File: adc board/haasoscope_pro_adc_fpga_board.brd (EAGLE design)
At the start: 224.5 x 160 mm, 580 parts, among them CN2 12Vin, IC1 ADC12DL2500ACF, IC10 TPS72325DBVR, IC13 LMH5401IRMST, IC14 LMH6401IRMZR, IC15 SN74AVC4T774PWR, IC17 DAC8562SDGSR, IC18 TLV9102IPWR, IC2 SN74AVC4T774PWR, IC21 LMH5401IRMST, IC22 TPS7A7200RGTR, IC23 TPS7A7200RGTR, IC24 TPS7A7200RGTR, IC25 TPS72325DBVR, IC26 TPS7A7200RGTR, IC27 TPS7A7200RGTR, IC28 TPS7A7200RGTR, IC29 LMH6401IRMZR, IC3 ADC122S021CIMM_NOPB, IC30 SN74AVC4T774PWR, IC33 TLV9102IPWR, IC4 TLV9102IPWR, IC5 EP4CE30F23C6N, IC6 EPCQ16ASI8N, IC7 TPS7A7200RGTR, IC8 FT232HQ, IC9 93LC56B, J1 2p-2.54, J10 8pin, J11 8pin, J13 8pin, J14 2x5, J15 test1, J2 test1, J3 2p-2.54, J30 2p-2.54, J31 2p-2.54, J32 2p-2.54, J33 2p-2.54, J34 2p-2.54, J35 2p-2.54, J36 2p-2.54, J37 2p-2.54, J39 2p-2.54, J4 2p-2.54, J40 2p-2.54, J41 2p-2.54, J42 2p-2.54, J43 2p-2.54, J44 2p-2.54, J45 2p-2.54, J46 2p-2.54, J8 8pin, K1 G6K-2F-RF-T-TR03_DC5, K2 G6K-2F-RF-T-TR03_DC5, K3 G6K-2F-RF-T-TR03_DC5, K4 G6K-2F-RF-T-TR03_DC5, K5 G6K-2F-RF-T-TR03_DC5, K6 TLP3475R_TP,F, K7 TLP3475R_TP,F, Q1 S8050, Q2 FDN340P, Q4 S8050, Q5 S8050, Q7 S8050, Q8 S8050, Q9 S8050, SW3 SKQGADE010, SW4 SKQGADE010, U2 ADF4350BCPZ, X1 USBC, Y2 OSCILLATORSMD-5X3, Y3 12MHz

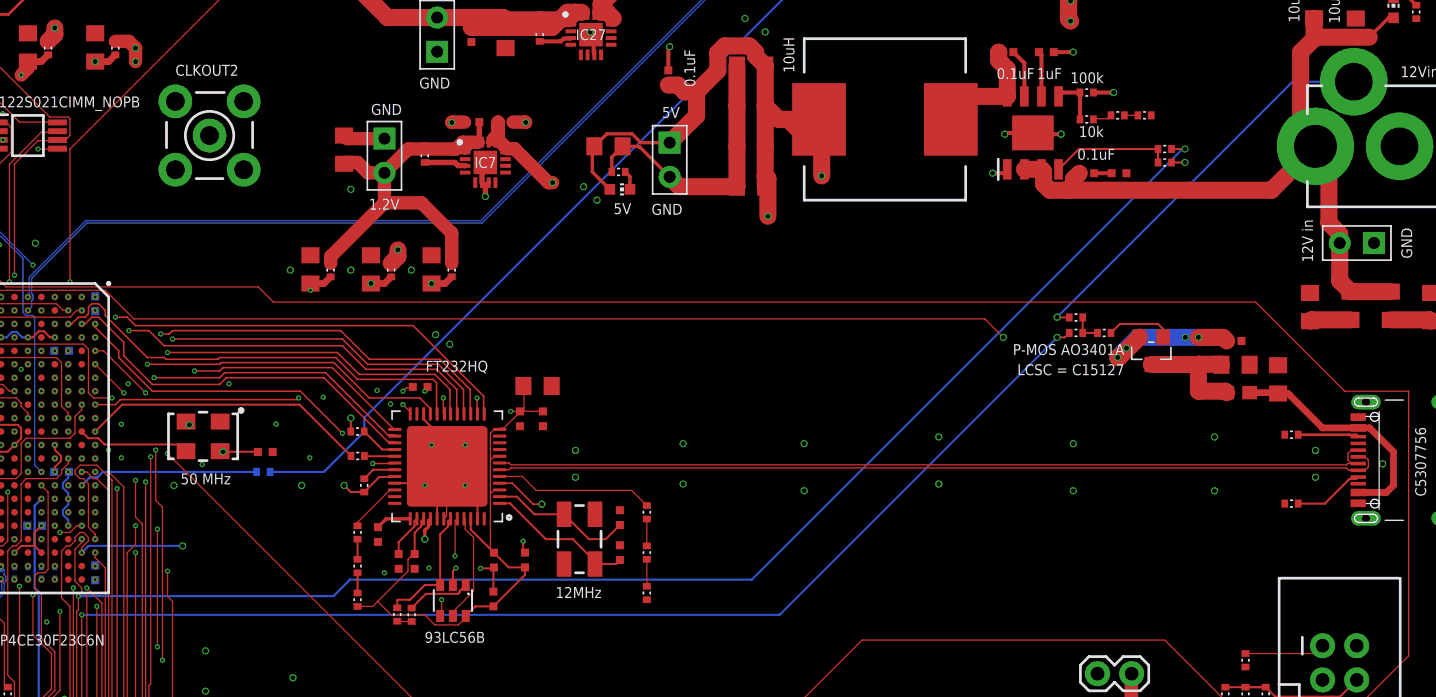
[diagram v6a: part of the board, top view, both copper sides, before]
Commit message: detect 12V and disconnect 5V from USB
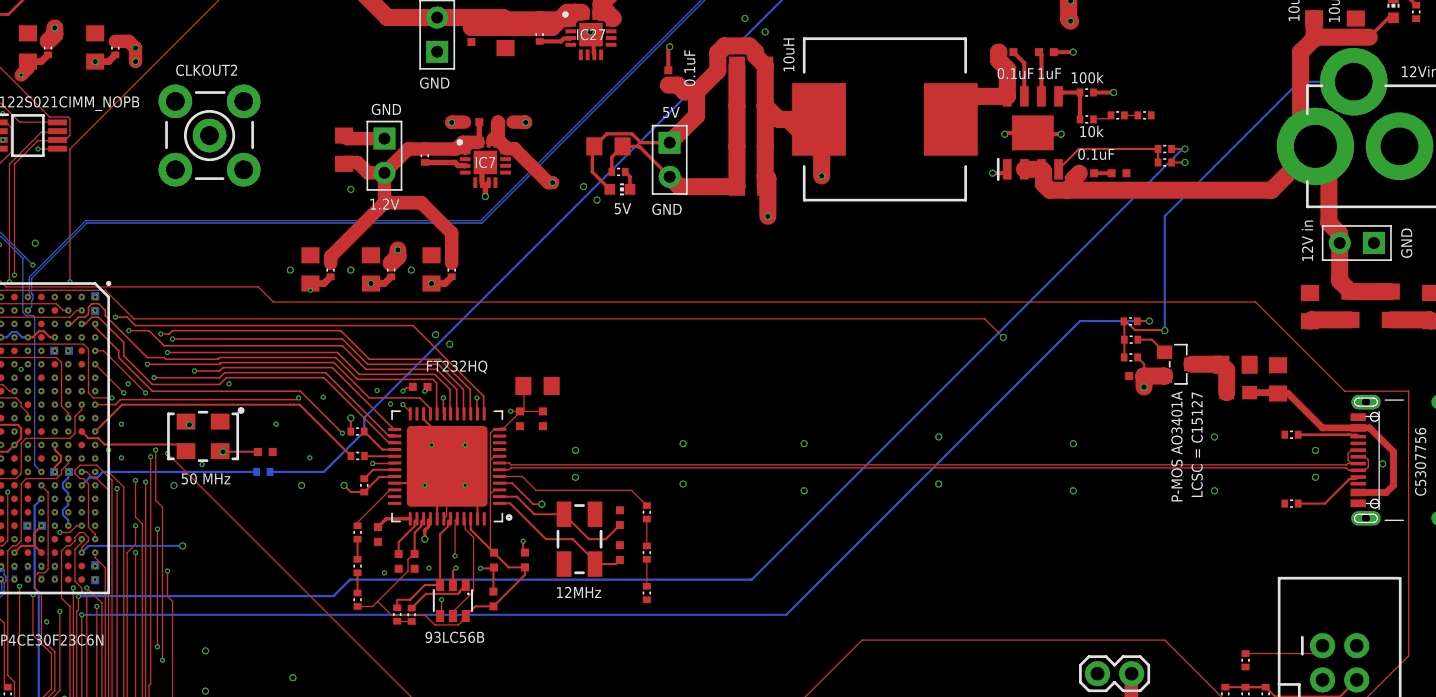
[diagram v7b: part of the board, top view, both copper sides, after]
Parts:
- moved C117 7.71 mm to (199.9, 84.1), turned to 0 degrees
- moved R237 5.05 mm to (199.5, 85.5)
- moved R238 4.15 mm to (199.5, 88.2), turned to 0 degrees
- moved Q2 2.24 mm to (203.0, 85.0), turned to 270 degrees
- moved R239 2.06 mm to (199.5, 86.8)
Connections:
- removed net 12VNOTCONNECTED: R237.P$2, R238.P$1, R239.P$1
- removed net N$64: CN2.GNDBREAK, R237.P$1
- new net 12VCONNECTED: CN2.GNDBREAK, R237.P$1, R238.P$1, R239.P$1
- net 5V: now also R237.P$2
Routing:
- net 12VCONNECTED: track 0.00 -> 32.7 mm, vias 0 -> 1
- net N$64: track 30.2 -> 0.00 mm, vias 1 -> 0
- net BOARDIN2: track 139.9 -> 147.1 mm
- net 5V: track 133.1 -> 126.0 mm, vias 26 -> 23
- net VBUSCLEAN: track 9.38 -> 4.44 mm
- net N$65: track 4.92 -> 2.37 mm
- net 12VNOTCONNECTED: track 2.25 -> 0.00 mm
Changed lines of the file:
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@@
 <element name="C115" library="Nordic_nRF" library_urn="urn:adsk.eagle:library:169009" package="RESC0402_N" package3d_urn="urn:adsk.eagle:package:2593732/1" value="0.1uF" x="143.517" y="72.347" smashed="yes" rot="R90"/>
 <element name="C116" library="Nordic_nRF" library_urn="urn:adsk.eagle:library:169009" package="RESC0402_N" package3d_urn="urn:adsk.eagle:package:2593732/1" value="0.1uF" x="154.0735" y="80.947" smashed="yes" rot="R90"/>
-<element name="C117" library="Nordic_nRF" library_urn="urn:adsk.eagle:library:169009" package="RESC0402_N" package3d_urn="urn:adsk.eagle:package:2593732/1" value="0.1uF" x="207.153" y="86.7345" smashed="yes" rot="R180"/>
+<element name="C117" library="Nordic_nRF" library_urn="urn:adsk.eagle:library:169009" package="RESC0402_N" package3d_urn="urn:adsk.eagle:package:2593732/1" value="0.1uF" x="199.897" y="84.1255" smashed="yes"/>
 <element name="C118" library="Nordic_nRF" library_urn="urn:adsk.eagle:library:169009" package="RESC0805_N" package3d_urn="urn:adsk.eagle:package:2593736/1" value="10uF" x="210.4235" y="83.8275" smashed="yes" rot="R270"/>
 <element name="C119" library="Nordic_nRF" library_urn="urn:adsk.eagle:library:169009" package="RESC0402_N" package3d_urn="urn:adsk.eagle:package:2593732/1" value="0.1uF" x="146.2455" y="70.347" smashed="yes" rot="R90"/>
@@
 <element name="R212" library="FlashPCB_Resistors" package="RES-0402" value="10k" x="202" y="100" smashed="yes" rot="R180"/>
 <element name="R236" library="FlashPCB_Resistors" package="RES-0402" value="1k" x="202" y="101" smashed="yes"/>
-<element name="Q2" library="Seeed-Transistor" library_urn="urn:adsk.eagle:library:477" package="SOT-23" package3d_urn="urn:adsk.eagle:package:33015/1" value="FDN340P" x="201" y="86" smashed="yes" rot="R180">
-<attribute name="LCSC" value="C15127" x="199" y="85" size="0.8128" layer="21" rot="R180" display="both"/>
-<attribute name="MPN" value="P-MOS AO3401A" x="199" y="86.5" size="0.8128" layer="21" rot="R180"/>
-</element>
-<element name="R237" library="FlashPCB_Resistors" package="RES-0402" value="10k" x="195.4" y="88.48" smashed="yes"/>
-<element name="R238" library="FlashPCB_Resistors" package="RES-0402" value="1k" x="195.4" y="87.33" smashed="yes" rot="R180"/>
-<element name="R239" library="FlashPCB_Resistors" package="RES-0402" value="10k" x="197.5" y="87.33" smashed="yes"/>
+<element name="Q2" library="Seeed-Transistor" library_urn="urn:adsk.eagle:library:477" package="SOT-23" package3d_urn="urn:adsk.eagle:package:33015/1" value="FDN340P" x="203" y="85" smashed="yes" rot="R270">
+<attribute name="LCSC" value="C15127" x="204" y="83" size="0.8128" layer="21" rot="R270" display="both"/>
+<attribute name="MPN" value="P-MOS AO3401A" x="202.5" y="83" size="0.8128" layer="21" rot="R270"/>
+</element>
+<element name="R237" library="FlashPCB_Resistors" package="RES-0402" value="10k" x="199.48" y="85.51" smashed="yes"/>
+<element name="R238" library="FlashPCB_Resistors" package="RES-0402" value="1k" x="199.46" y="88.19" smashed="yes"/>
+<element name="R239" library="FlashPCB_Resistors" package="RES-0402" value="10k" x="199.5" y="86.83" smashed="yes"/>
 </elements>
 <signals>
@@
 <via x="121.5" y="29.875" extent="1-16" drill="0.2"/>
 <contactref element="R238" pad="P$2"/>
-<wire x1="194.9" y1="87.33" x2="194.57" y2="87" width="0.1524" layer="1"/>
-<wire x1="194.57" y1="87" x2="194" y2="87" width="0.1524" layer="1"/>
-<via x="194" y="87" extent="1-16" drill="0.35"/>
-<wire x1="194" y1="87" x2="173.375" y2="66.375" width="0.1524" layer="16"/>
-<wire x1="173.375" y1="66.375" x2="121.5" y2="66.375" width="0.1524" layer="16"/>
+<via x="200.86" y="88.21" extent="1-16" drill="0.35"/>
+<wire x1="200.86" y1="88.21" x2="195.71" y2="88.21" width="0.1524" layer="16"/>
+<wire x1="195.71" y1="88.21" x2="173.875" y2="66.375" width="0.1524" layer="16"/>
+<wire x1="173.875" y1="66.375" x2="121.5" y2="66.375" width="0.1524" layer="16"/>
+<wire x1="199.96" y1="88.19" x2="199.98" y2="88.21" width="0.1524" layer="1"/>
+<wire x1="200.86" y1="88.21" x2="199.98" y2="88.21" width="0.1524" layer="1"/>
 </signal>
 <signal name="BOARDIN3">
@@
 <vertex x="-9.5" y="-11.5"/>
 </polygon>
-<via x="204.5" y="87" extent="1-16" drill="0.35"/>
+<via x="200.46" y="83.31" extent="1-16" drill="0.35"/>
 <via x="172.5" y="96" extent="1-16" drill="0.35"/>
 <via x="176.5" y="99" extent="1-16" drill="0.35"/>
@@
 <wire x1="194.85615" y1="110.64385" x2="195" y2="110.5" width="1.27" layer="1"/>
 <contactref element="JST_FAN" pad="1"/>
-<wire x1="204.5" y1="87" x2="206.3375" y2="87" width="1.27" layer="1"/>
-<wire x1="206.3375" y1="87" x2="206.603" y2="86.7345" width="1.27" layer="1"/>
+<wire x1="200.447" y1="84.1255" x2="200.46" y2="84.1125" width="1.27" layer="1"/>
+<wire x1="200.46" y1="84.1125" x2="200.46" y2="83.31" width="1.27" layer="1"/>
 <contactref element="K1" pad="1"/>
 <contactref element="K2" pad="1"/>
@@
 <wire x1="200.8" y1="17.7" x2="200.8" y2="13.47" width="1.016" layer="1"/>
 <contactref element="Q2" pad="2"/>
-<wire x1="200.111" y1="87.016" x2="198.595" y2="85.5" width="1.27" layer="1"/>
-<wire x1="198.595" y1="85.5" x2="198.5" y2="85.5" width="1.27" layer="1"/>
-<via x="198.5" y="85.5" extent="1-16" drill="0.35"/>
-<wire x1="198.5" y1="85.5" x2="200" y2="87" width="1.27" layer="16"/>
-<wire x1="200" y1="87" x2="204.5" y2="87" width="1.27" layer="16"/>
-<via x="199.15" y="86.2" extent="1-16" drill="0.35"/>
-<via x="203.53" y="87" extent="1-16" drill="0.35"/>
+<contactref element="R237" pad="P$2"/>
+<wire x1="199.98" y1="85.51" x2="200.46" y2="85.03" width="0.1524" layer="1"/>
+<wire x1="200.46" y1="85.03" x2="200.46" y2="84.1125" width="0.1524" layer="1"/>
+<wire x1="200.447" y1="84.1255" x2="201.9695" y2="84.1255" width="1.27" layer="1"/>
+<wire x1="201.9695" y1="84.1255" x2="201.984" y2="84.111" width="1.27" layer="1"/>
 </signal>
 <signal name="COIL1-">
@@
 <contactref element="FB2" pad="2"/>
 <contactref element="C126" pad="2"/>
-<wire x1="204.5" y1="85" x2="206.1725" y2="85" width="1.27" layer="1"/>
-<wire x1="206.1725" y1="85" x2="206.2085" y2="84.964" width="1.27" layer="1"/>
-<wire x1="204.5" y1="83" x2="206.496" y2="83" width="1.27" layer="1"/>
-<wire x1="206.496" y1="83" x2="206.6045" y2="82.8915" width="1.27" layer="1"/>
 <contactref element="Q2" pad="3"/>
-<wire x1="204.5" y1="85" x2="204.484" y2="84.984" width="1.27" layer="1"/>
-<wire x1="204.484" y1="84.984" x2="201" y2="84.984" width="1.27" layer="1"/>
-<wire x1="204.5" y1="85" x2="204.5" y2="83" width="1.27" layer="1"/>
+<wire x1="204.016" y1="85" x2="206.1725" y2="85" width="1.27" layer="1"/>
+<wire x1="206.1725" y1="85" x2="206.2085" y2="84.964" width="1.27" layer="1"/>
+<wire x1="206.2085" y1="84.964" x2="206.6045" y2="84.568" width="1.27" layer="1"/>
+<wire x1="206.6045" y1="84.568" x2="206.6045" y2="82.8915" width="1.27" layer="1"/>
 </signal>
-<signal name="12VNOTCONNECTED">
-<contactref element="R237" pad="P$2"/>
+<signal name="12VCONNECTED">
 <contactref element="R238" pad="P$1"/>
 <contactref element="R239" pad="P$1"/>
-<wire x1="195.9" y1="88.48" x2="195.9" y2="87.33" width="0.1524" layer="1"/>
-<wire x1="195.9" y1="87.33" x2="197" y2="87.33" width="0.1524" layer="1"/>
-</signal>
-<signal name="N$64">
 <contactref element="CN2" pad="GNDBREAK"/>
 <contactref element="R237" pad="P$1"/>
-<wire x1="194.9" y1="88.48" x2="194.02" y2="88.48" width="0.1524" layer="1"/>
-<wire x1="194.02" y1="88.48" x2="194" y2="88.5" width="0.1524" layer="1"/>
-<via x="194" y="88.5" extent="1-16" drill="0.35"/>
-<wire x1="194" y1="88.5" x2="211.5" y2="106" width="0.1524" layer="16"/>
-<wire x1="211.5" y1="106" x2="216.05" y2="106" width="0.1524" layer="16"/>
+<via x="202" y="87.5" extent="1-16" drill="0.35"/>
+<wire x1="216.05" y1="106" x2="212" y2="106" width="0.1524" layer="16"/>
+<wire x1="212" y1="106" x2="202" y2="96" width="0.1524" layer="16"/>
+<wire x1="202" y1="96" x2="202" y2="87.5" width="0.1524" layer="16"/>
+<wire x1="198.96" y1="88.19" x2="199" y2="88.15" width="0.1524" layer="1"/>
+<wire x1="199" y1="88.15" x2="199" y2="86.83" width="0.1524" layer="1"/>
+<wire x1="199" y1="86.83" x2="199" y2="85.53" width="0.1524" layer="1"/>
+<wire x1="199" y1="85.53" x2="198.98" y2="85.51" width="0.1524" layer="1"/>
+<wire x1="199.16263125" y1="88.15" x2="199" y2="88.15" width="0.1524" layer="1"/>
+<wire x1="202" y1="87.5" x2="201.9582" y2="87.5418" width="0.1524" layer="1"/>
+<wire x1="201.9582" y1="87.5418" x2="199.77083125" y2="87.5418" width="0.1524" layer="1"/>
+<wire x1="199.77083125" y1="87.5418" x2="199.16263125" y2="88.15" width="0.1524" layer="1"/>
 </signal>
 <signal name="N$65">
 <contactref element="Q2" pad="1"/>
 <contactref element="R239" pad="P$2"/>
-<wire x1="198" y1="87.33" x2="198.67" y2="88" width="0.1524" layer="1"/>
-<wire x1="198.67" y1="88" x2="201.5" y2="88" width="0.1524" layer="1"/>
-<wire x1="201.5" y1="88" x2="201.889" y2="87.611" width="0.1524" layer="1"/>
-<wire x1="201.889" y1="87.611" x2="201.889" y2="87.016" width="0.1524" layer="1"/>
+<wire x1="200" y1="86.83" x2="201.043" y2="86.83" width="0.1524" layer="1"/>
+<wire x1="201.043" y1="86.83" x2="201.984" y2="85.889" width="0.1524" layer="1"/>
 </signal>
 </signals>

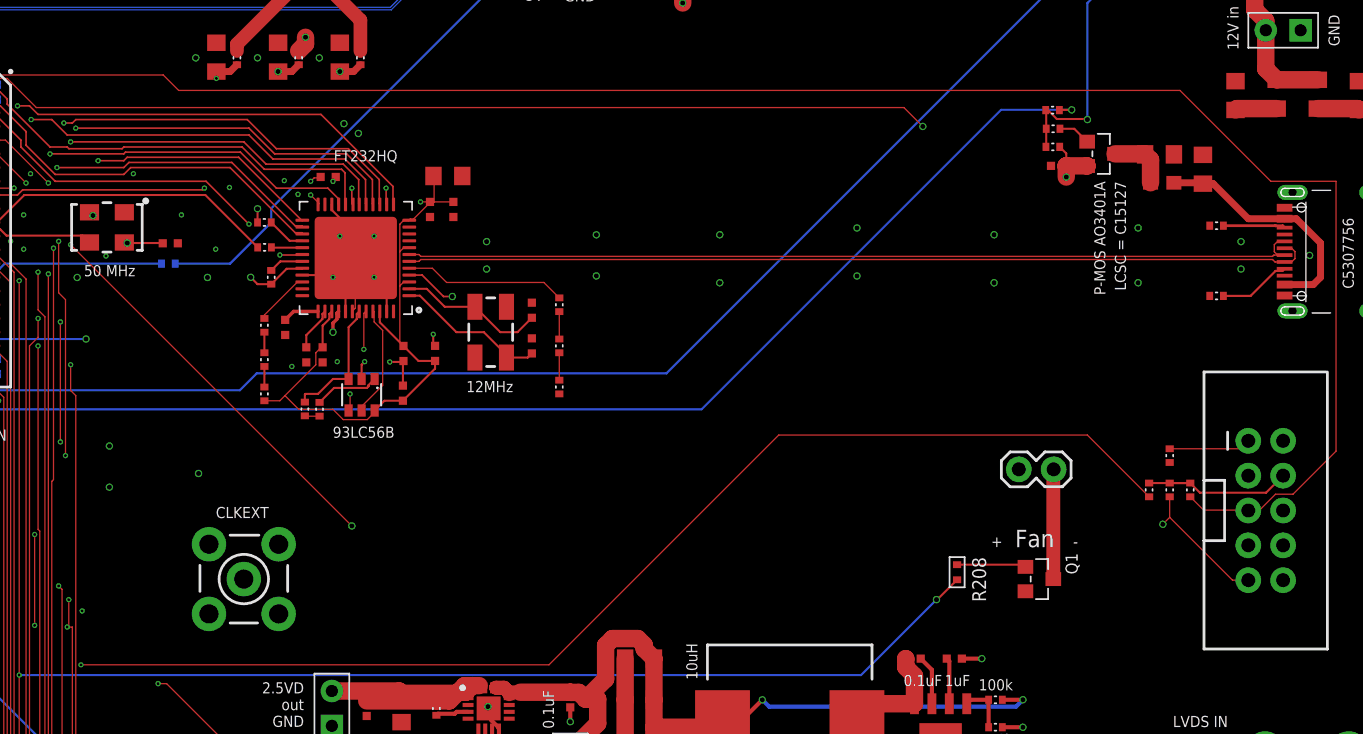
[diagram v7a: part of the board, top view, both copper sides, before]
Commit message: Add comparitors of CC1/2 to 0.7V for USB C power detection
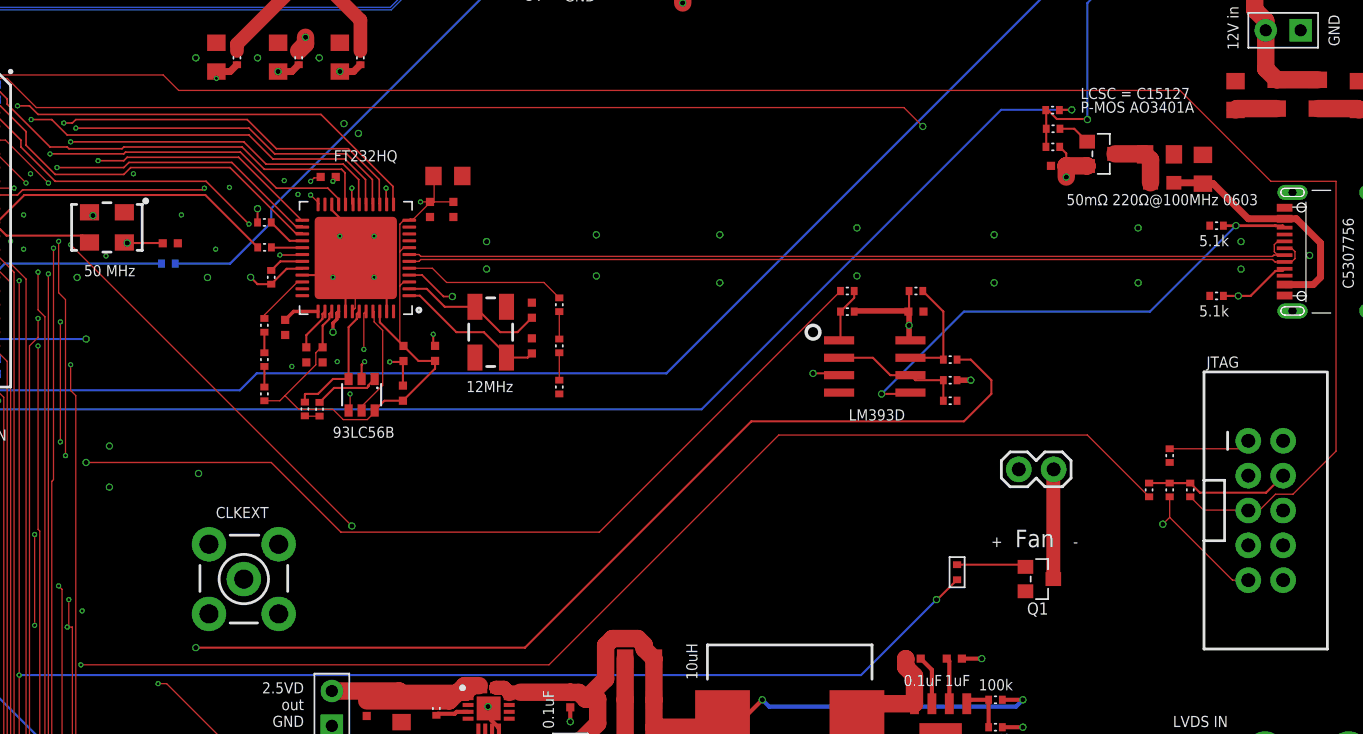
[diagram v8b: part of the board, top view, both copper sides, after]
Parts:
- added C80: 0.1uF, Nordic_nRF:RESC0402_N
- added IC11: LM393D, linear:SO08
- added R240, R241, R244: 10k, FlashPCB_Resistors:RES-0402
- added R242, R243: 1k, FlashPCB_Resistors:RES-0402
- added R245: 39k, FlashPCB_Resistors:RES-0402
- renumbered J14 to JTAG
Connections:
- new net 0V7REF: IC11.2, IC11.6, R244.P$1, R245.P$2
- new net CC1COMPOUT: IC11.1, R240.P$1, R242.P$1
- new net CC2COMPOUT: IC11.7, R241.P$1, R243.P$1
- net 3V3: now also C80.2, IC11.8, R240.P$2, R241.P$2, R244.P$2
- net BOARDIN0: now also R242.P$2
- net BOARDIN1: now also R243.P$2
- net CC1: now also IC11.3
- net CC2: now also IC11.5
- net GND: now also C80.1, IC11.4, R245.P$1
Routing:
- net BOARDIN1: track 60.8 -> 157.6 mm, vias 3 -> 4
- net BOARDIN0: track 54.4 -> 129.8 mm, vias 3 -> 4
- net CC1: track 5.28 -> 40.6 mm, vias 0 -> 2
- net CC2: track 4.52 -> 37.6 mm, vias 0 -> 2
- net 3V3: track 155.5 -> 165.5 mm, vias 23 -> 25
- net 0V7REF: track 0.00 -> 9.78 mm
- net CC2COMPOUT: track 0.00 -> 8.08 mm
- net CC1COMPOUT: track 0.00 -> 4.05 mm
